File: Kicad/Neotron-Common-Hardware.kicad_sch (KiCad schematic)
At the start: 17 parts, among them J101 Neotron-Expansion-Slot, J102 Neotron-Expansion-Slot, J103 Neotron-Expansion-Slot, J104 Neotron-Expansion-Slot, U101 Neotron-CPU

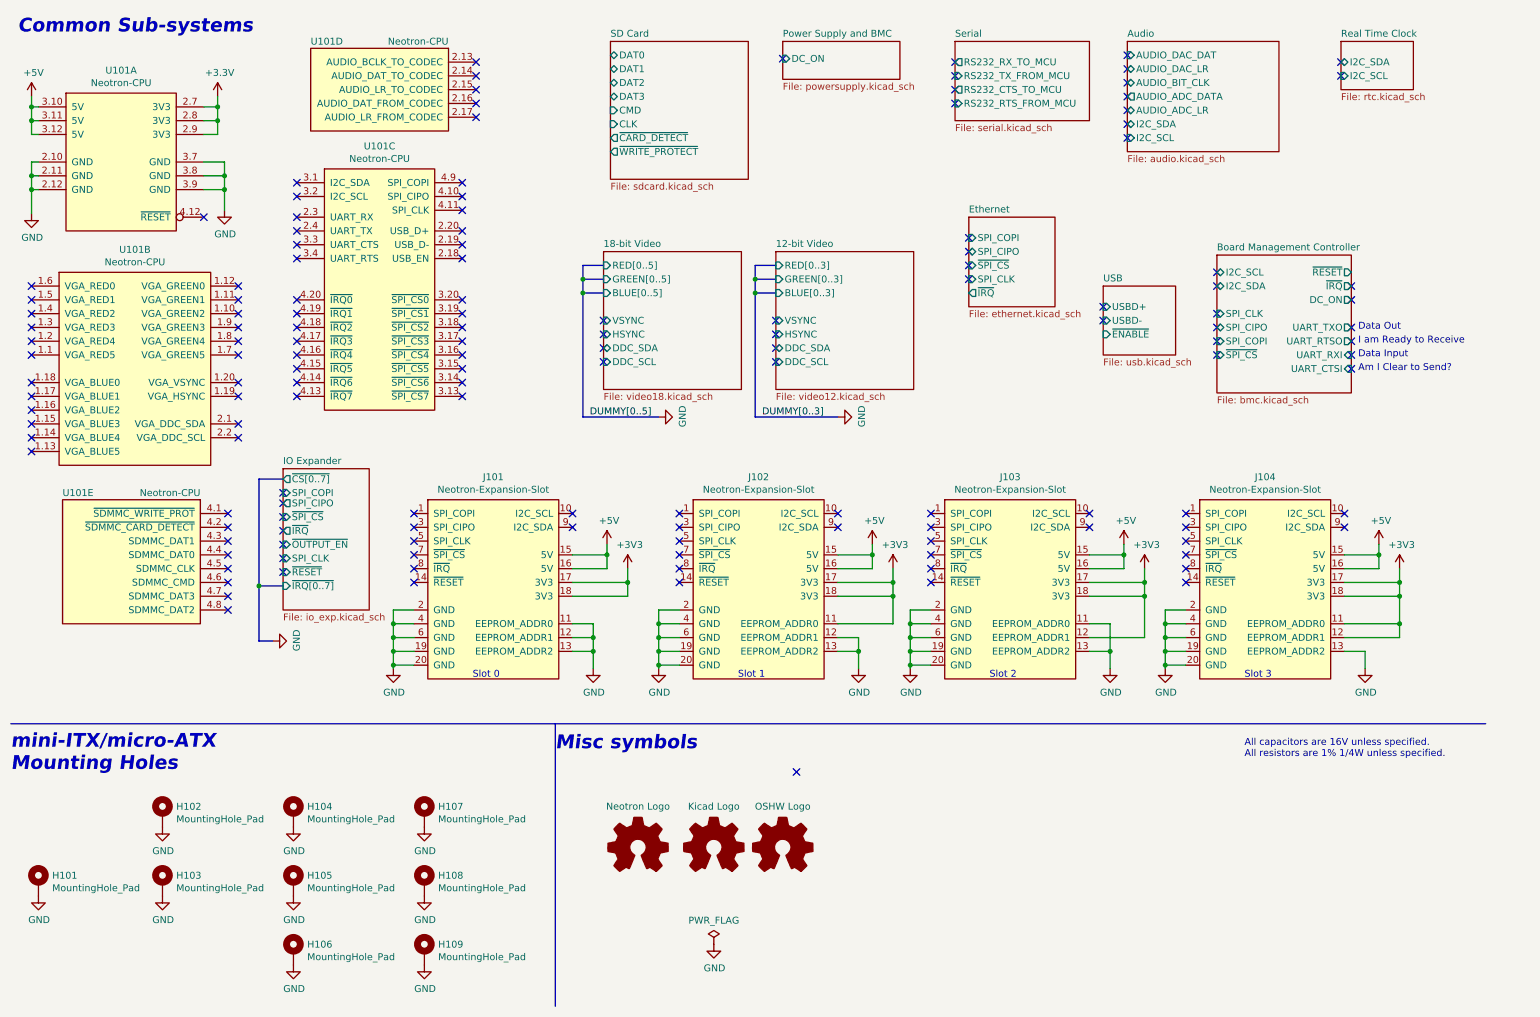
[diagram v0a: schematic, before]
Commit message: Update schematic files to Kicad 6.
Had to fix some symbols which didn't have perfect matches in K6.
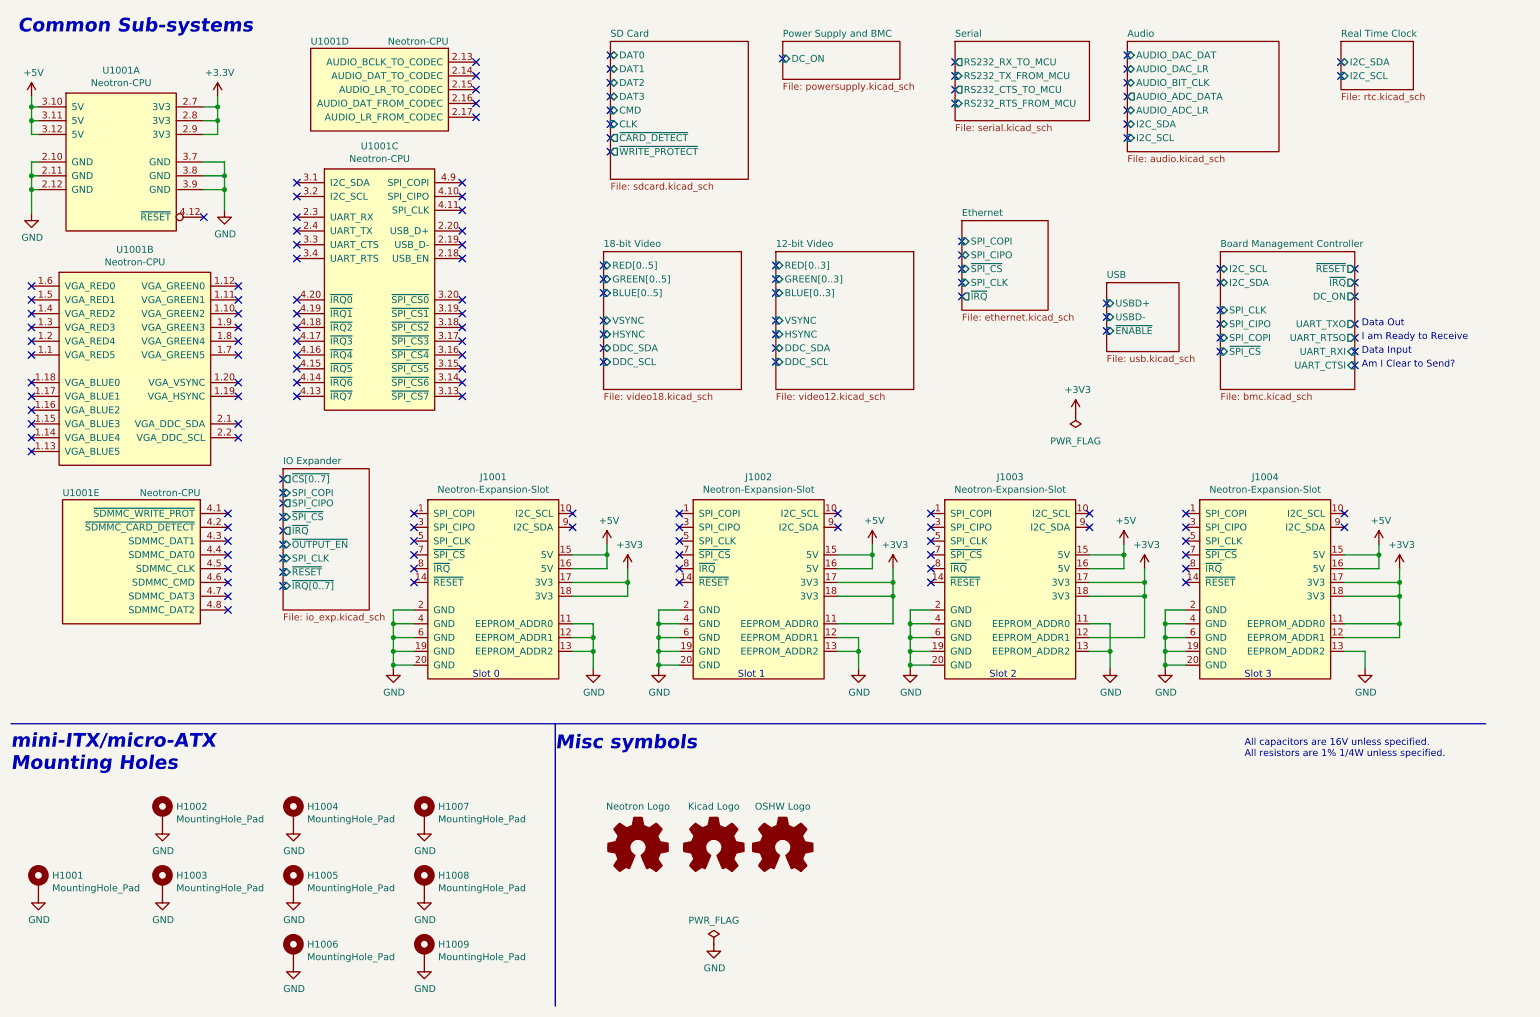
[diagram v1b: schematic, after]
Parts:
- renumbered H101 to H1001, H102 to H1002, H103 to H1003, H104 to H1004, H105 to H1005, H106 to H1006, H107 to H1007, H108 to H1008, H109 to H1009, J101 to J1001, J102 to J1002, J103 to J1003, J104 to J1004, LOGO101 to LOGO1001, LOGO102 to LOGO1002, LOGO103 to LOGO1003, U101 to U1001
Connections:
- net +3V3: no longer U1001.2.7 (3V3), U1001.2.8 (3V3), U1001.2.9 (3V3)
- new net +3.3V: U1001.2.7 (3V3), U1001.2.8 (3V3), U1001.2.9 (3V3)
- no-connect marks 144 -> 162

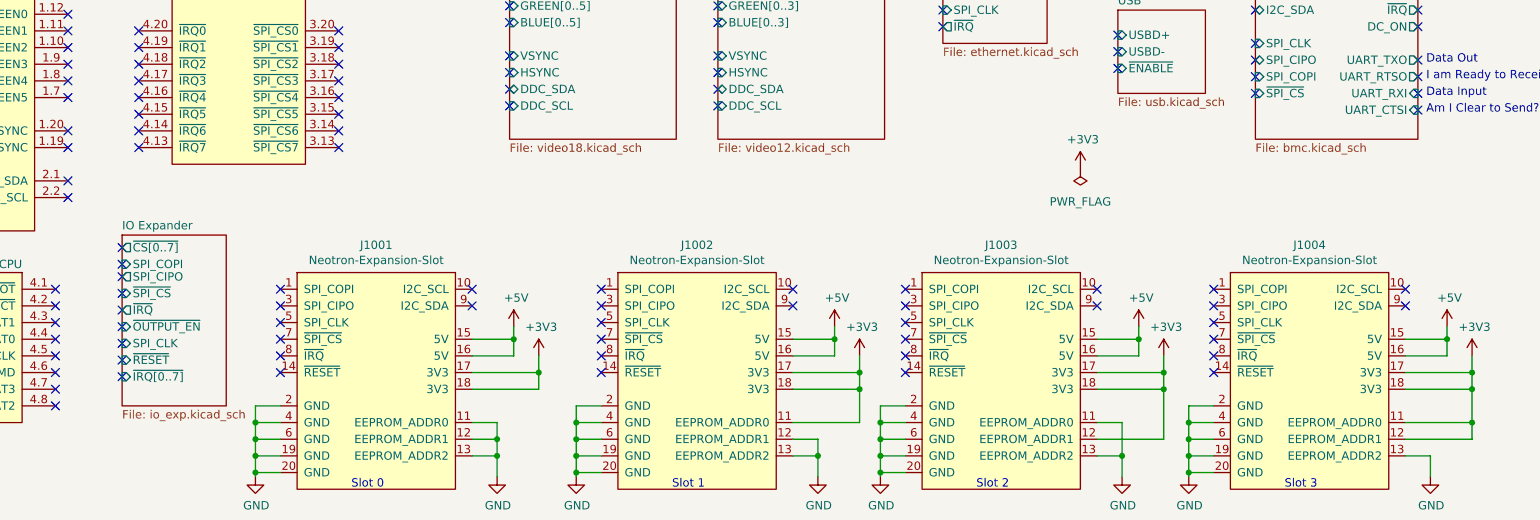
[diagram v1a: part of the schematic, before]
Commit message: Imported sheets from Neotron Pico.
Standardised on +3V3 not +3.3V
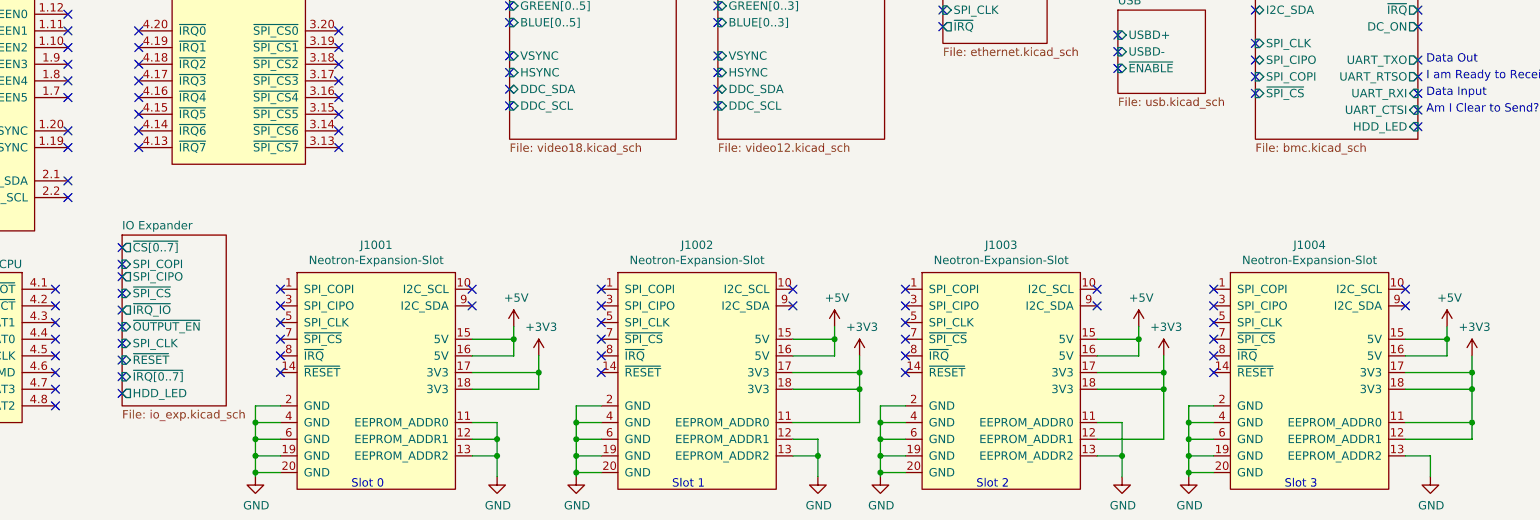
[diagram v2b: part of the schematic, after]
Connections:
- net +3.3V is gone; now on net +3V3: U1001.2.7 (3V3), U1001.2.8 (3V3), U1001.2.9 (3V3)
- no-connect marks 162 -> 164
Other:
- sheet Board Management Controller ports: added HDD_LED; removed none
- sheet IO Expander ports: added HDD_LED, ~{IRQ_IO}; removed ~{IRQ}

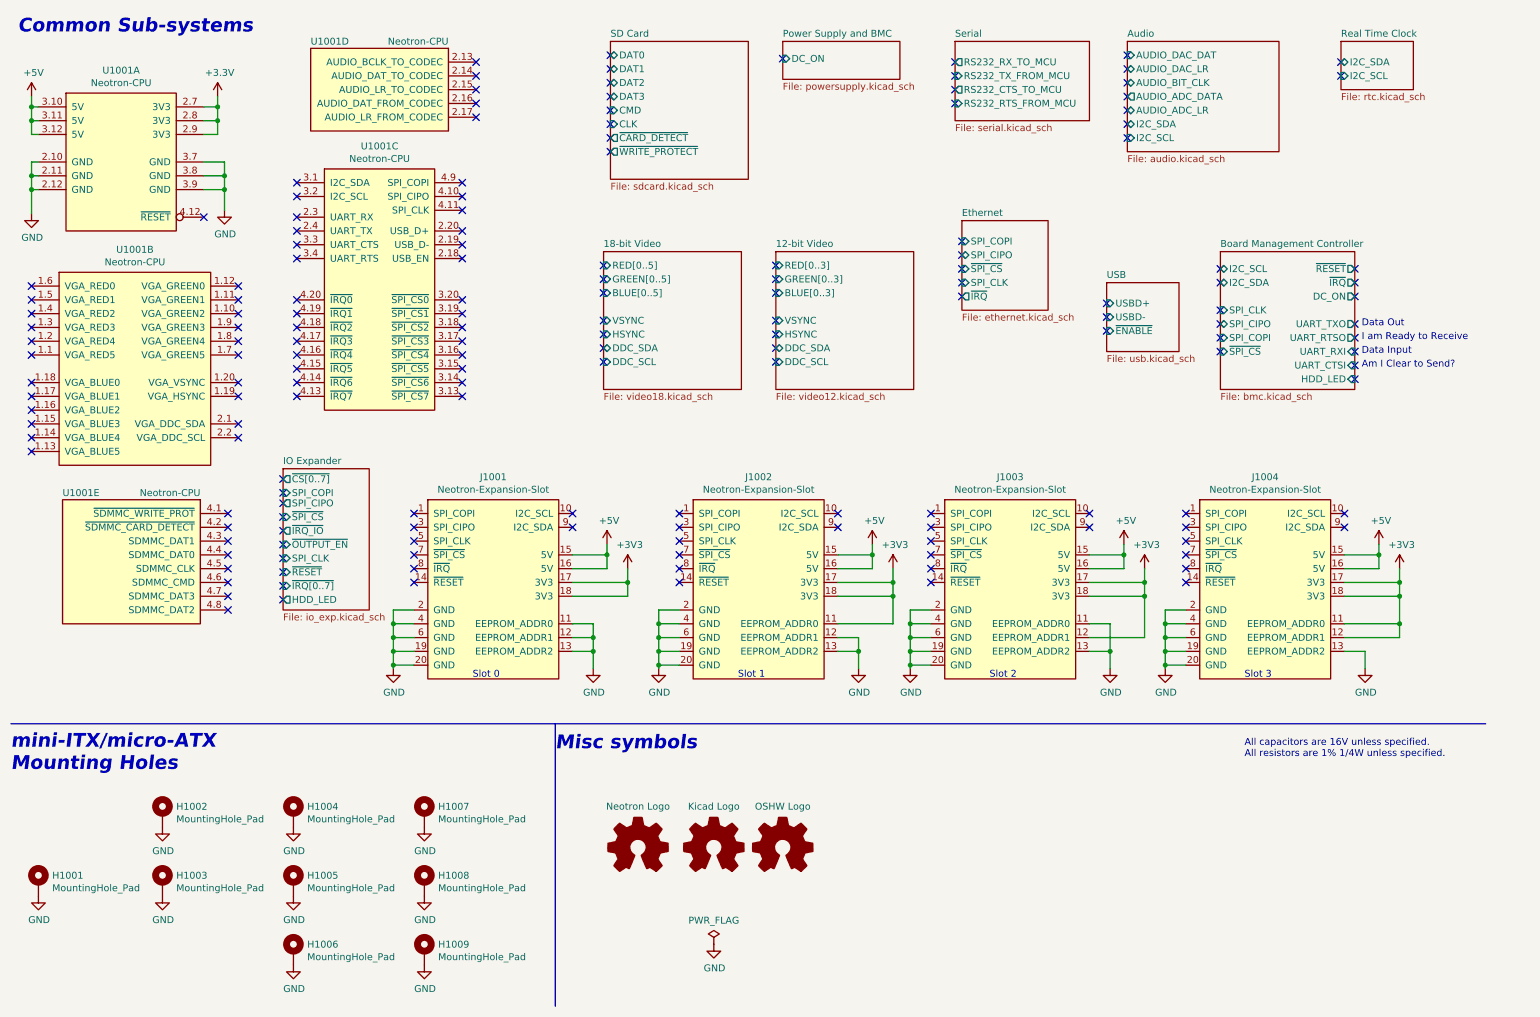
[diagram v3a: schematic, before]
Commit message: Re-imported from Neotron Pico v1.1.
This time I deleted the sheets from the top level and then re-added pointing at the new files. I also reset the PCB dimensions to match the Neotron Pico.

This seems to have done a better job importing footprints.
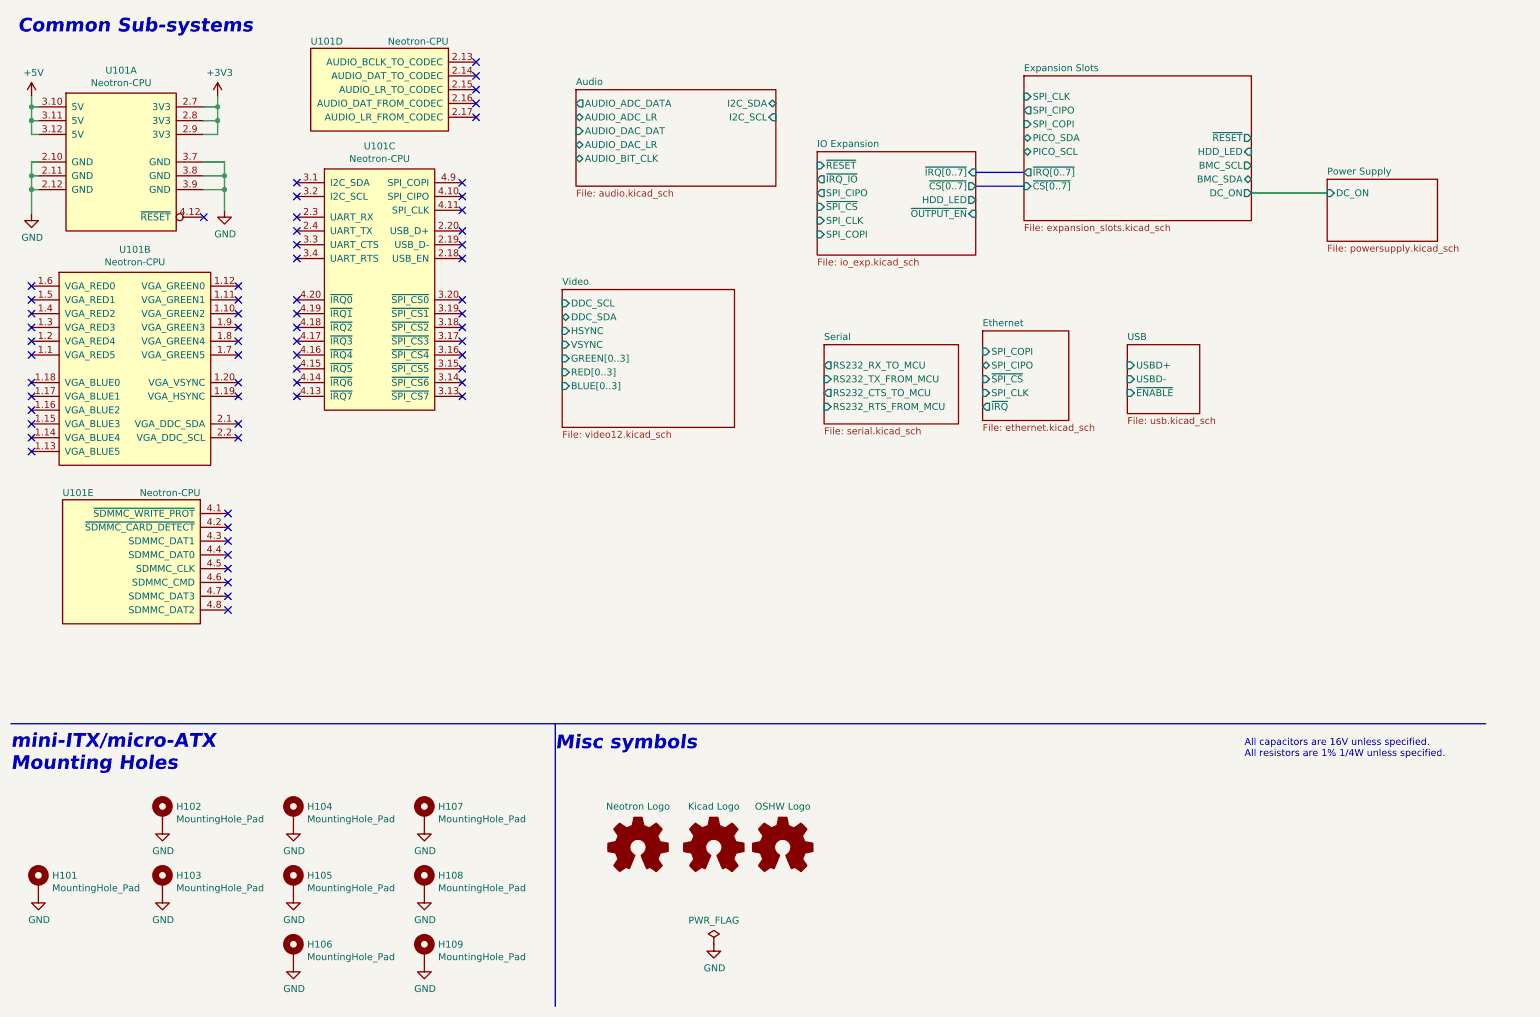
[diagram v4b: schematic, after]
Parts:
- removed J1001, J1002, J1003, J1004: Neotron-Expansion-Slot, Neotron-Common-Hardware:Neotron-Expansion-Slot, symbol Neotron-Common-Hardware:Neotron-Expansion-Slot
- renumbered H1001 to H101, H1002 to H102, H1003 to H103, H1004 to H104, H1005 to H105, H1006 to H106, H1007 to H107, H1008 to H108, H1009 to H109, LOGO1001 to LOGO101, LOGO1002 to LOGO102, LOGO1003 to LOGO103, U1001 to U101
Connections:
- no-connect marks 164 -> 64
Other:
- removed sheet 12-bit Video
- removed sheet 18-bit Video
- removed sheet Board Management Controller
- removed sheet IO Expander
- removed sheet Power Supply and BMC
- removed sheet Real Time Clock
- removed sheet SD Card
- added sheet Expansion Slots (expansion_slots.kicad_sch)
- added sheet IO Expansion (io_exp.kicad_sch)
- added sheet Power Supply (powersupply.kicad_sch)
- added sheet Video (video12.kicad_sch)
- note removed: "Am I Clear to Send?"
- note removed: "Data Input"
- note removed: "Data Out"
- note removed: "I am Ready to Receive"
- note removed: "Slot 0"
- note removed: "Slot 1"
- note removed: "Slot 2"
- note removed: "Slot 3"
